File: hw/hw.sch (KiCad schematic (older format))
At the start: 32 parts, among them U1 74LS32, U10 74LS74, U2 Z80CPU, U3 74LS138, U4 74LS08, U5 CY7C199, U6 74LS299, U7 74HCT574, U8 74LS161, U9 74LS245, X1 CXO_DIP8

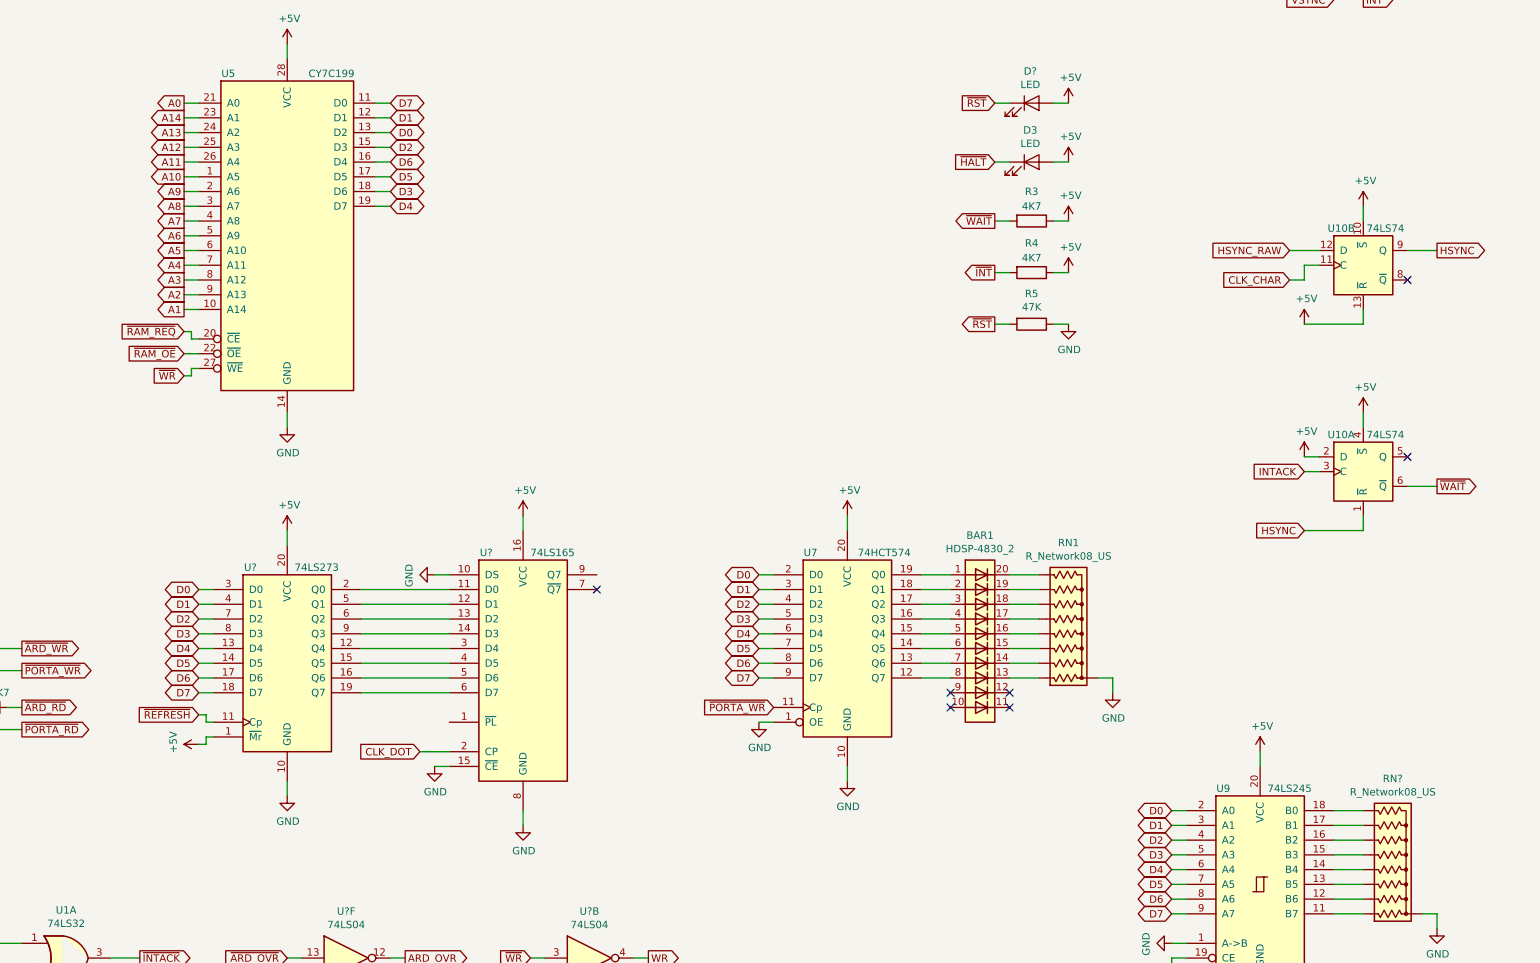
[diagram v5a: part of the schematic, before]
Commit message: start to get video signal
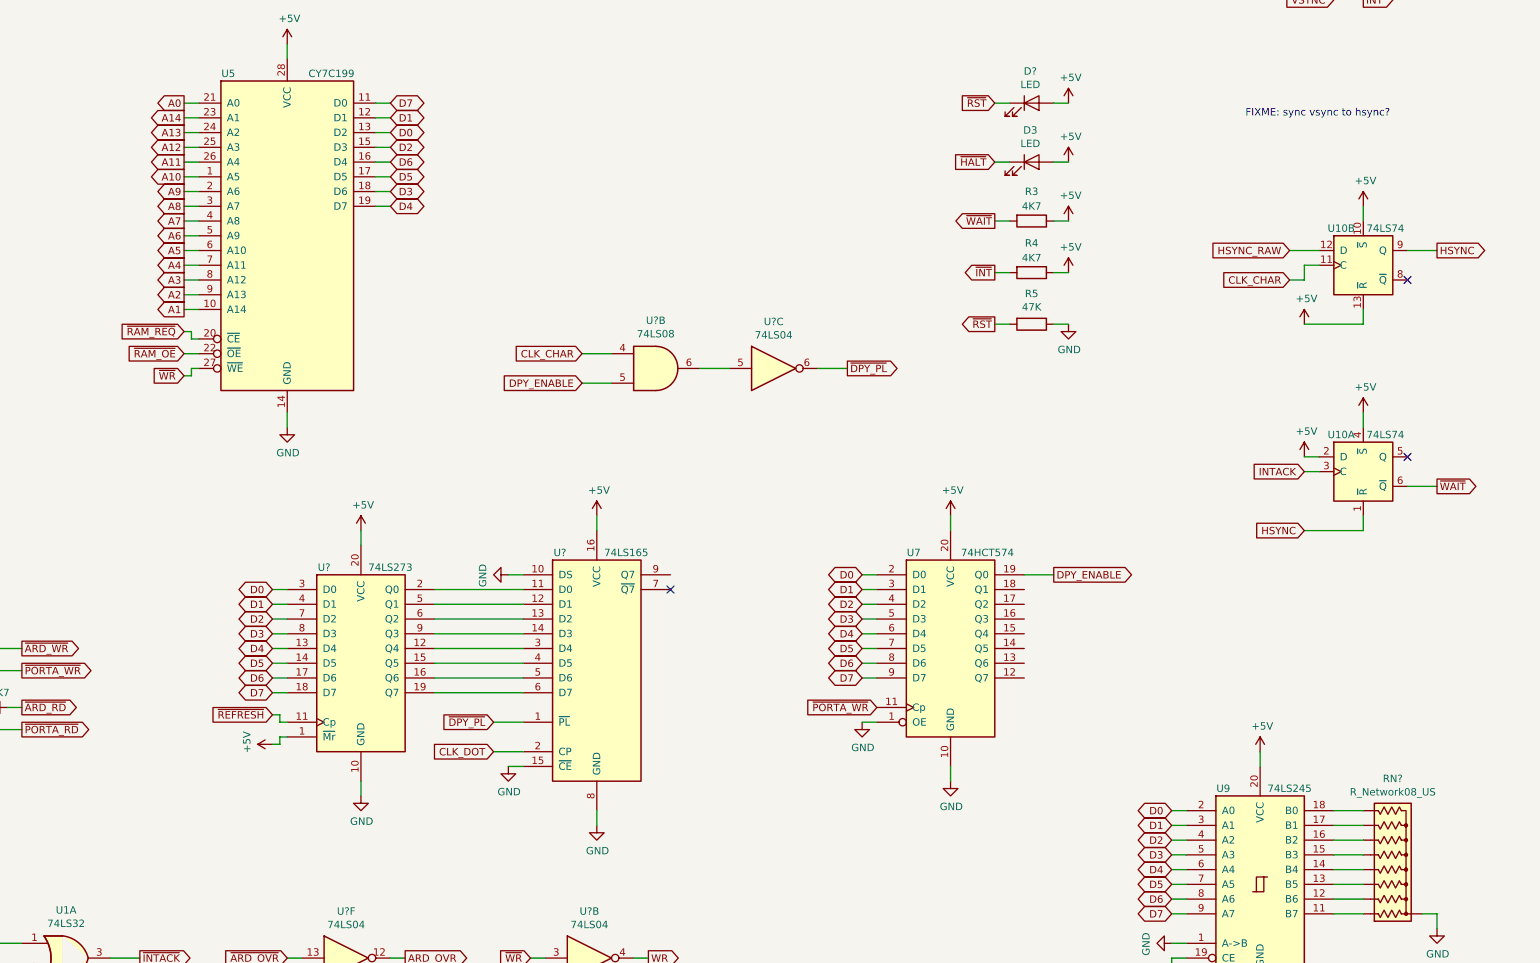
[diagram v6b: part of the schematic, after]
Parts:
- removed BAR1: HDSP-4830_2, Display:HDSP-4830, symbol LED:HDSP-4830_2
- removed RN1: R_Network08_US, Resistor_THT:R_Array_SIP9, symbol Device:R_Network08_US
- added U?: 74LS08, symbol 74xx:74LS08
- added U?: 74LS04, symbol 74xx:74LS04
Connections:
- net CLK_CHAR: now also U?.4
- net DPY_ENABLE: now reaches U7.19 (Q0)
- net DPY_ENABLE: now also U?.5
- net ~DPY_PL: now reaches U?.1 (~PL)
- net ~DPY_PL: now also U?.6
- new net: U?.5, U?.6
- no-connect marks 31 -> 27
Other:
- note added: "FIXME: sync vsync to hsync?"
- moved on the sheet: U7, U?

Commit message: working video signal(!)
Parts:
- added J?: DB15_Female_HighDensity_MountingHoles, symbol Connector:DB15_Female_HighDensity_MountingHoles
- added R? (x3): 470, symbol Device:R
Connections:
- net GND: now also J?.0, J?.10, J?.5, J?.6, J?.7, J?.8
- net HSYNC: now also J?.13
- net VSYNC: now also J?.14
- net at U?.9 (Q7): now also R?.2, R?.2, R?.2
- new net: J?.1, R?.1
- new net: J?.2, R?.1
- new net: J?.3, R?.1
- no-connect marks 27 -> 32
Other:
- moved on the sheet: RN?, U7, U9

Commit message: getting there
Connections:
- net CLK_CHAR: no longer U?.4
- net VSYNC: no longer R4.2, U2.16 (~INT~)
- net CHAR_TC: now reaches U8.15 (TC)
- net CHAR_TC: now also U?.4
- net ~INT: now reaches A1.22 (A3)
- net ~INT: now also R4.2, U2.16 (~INT~)
- no-connect marks 32 -> 30
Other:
- note removed: "FIXME: this should be delayed as it triggers at the start of the back porch"
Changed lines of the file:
@@
 Wire Wire Line
 	2400 10200 2300 10200
-Text GLabel 12700 800  0    50   Input ~ 0
-VSYNC
-Text GLabel 12900 800  2    50   Output ~ 0
-~INT
-Wire Wire Line
-	12700 800  12900 800
-Text Notes 13150 800  0    50   ~ 0
-FIXME: this should be delayed as it triggers at the start of the back porch
 Text GLabel 10400 2650 0    50   Output ~ 0
 ~INT
@@
 	1    0    0    -1
 $EndComp
-NoConn ~ 1300 10100
 Wire Wire Line
 	4700 9600 5600 9600
@@
 	9700 8100 9800 8100
 Connection ~ 9800 8100
-NoConn ~ 11400 9300
-Text GLabel 7600 3200 0    50   Input ~ 0
-CLK_CHAR
 Wire Wire Line
 	7000 5700 7200 5700
@@
 Wire Wire Line
 	8300 4900 8300 5100
+Text GLabel 1000 10100 0    50   Output ~ 0
+~INT
+Wire Wire Line
+	1300 10100 1000 10100
+Text GLabel 11600 9600 2    50   Output ~ 0
+CHAR_TC
+Wire Wire Line
+	11400 9300 11500 9300
+Wire Wire Line
+	11500 9300 11500 9600
+Wire Wire Line
+	11500 9600 11600 9600
+Text GLabel 7600 3200 0    50   Input ~ 0
+CHAR_TC
 $EndSCHEMATC
